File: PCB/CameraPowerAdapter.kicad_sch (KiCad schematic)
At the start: 1 part, among them U1 LT8390EFE#PBF

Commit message: Updated Schematic
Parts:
- added C10, C16, C17, C9: C, symbol Device:C
- added C11, C12, C13, C14: 100n, symbol Device:C
- added C15: 4.7u, symbol Device:C
- added C8: 1u, symbol Device:C
- added L1: L, symbol Device:L
- added Q3, Q4, Q5, Q6: NCEP40T11G, easyeda2kicad:DFN-8_L5.1-W5.7-P1.27-LS6.1-BL, symbol easyeda2kicad:NCEP40T11G
- added R10: 499k, symbol Device:R
- added R5: R, symbol Device:R
- added R8: 365k, symbol Device:R
- added R9: 56.2k, symbol Device:R
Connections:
- net GND: now reaches U1.10 (TEST)
- net GND: now also U1.29 (GND), C11.2, C12.2, C13.2, C14.2, C16.2, C17.2, C8.2, C9.2, R9.2
- net at U1.11 (LOADEN): now also U1.12 (Vref), U1.13 (CTRL), C16.1, R10.2
- net at U1.16 (ISMON): now also C17.1
- net PGOOD: now reaches U1.17 (PGOOD)
- net at U1.18 (SS): now also C9.1, R10.1
- net RT: now reaches U1.21 (RT)
- net SYNC/SPRD: now reaches U1.22 (SYNC/SPRD)
- net SYNC/SPRD: now also C15.1
- net INTVcc: now reaches U1.8 (INTVcc)
- net INTVcc: now also C15.2
- net BG1: now reaches U1.1 (BG1)
- net BG1: now also Q4.4 (G)
- net ISP: now reaches U1.14 (ISP)
- net ISN: now reaches U1.15 (ISN)
- net FB: now reaches U1.19 (FB)
- net at U1.2 (BST1): now also C10.2
- net TG2: now reaches U1.25 (TG2)
- net SW2: now reaches U1.26 (SW2)
- net SW2: now also L1.2
- net BST2: now reaches U1.27 (BST2)
- net BG2: now reaches U1.28 (BG2)
- net SW1: now reaches U1.3 (SW1)
- net SW1: now also U1.5 (LSP), C10.1, Q3.4 (G), R5.1
- net TG1: now reaches U1.4 (TG1)
- net TG1: now also Q6.4 (G)
- net at U1.6 (LSN): now also L1.1, R5.2
- net VOUT: now reaches U1.7 (Vin)
- net VOUT: now also C11.1, C12.1, C13.1, C14.1, C8.1, R8.1
- net EN/UVLO: now reaches U1.9 (EN/UVLO)
- net EN/UVLO: now also R8.2, R9.1
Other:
- note added: "Boost Side"
- note added: "Buck Side"

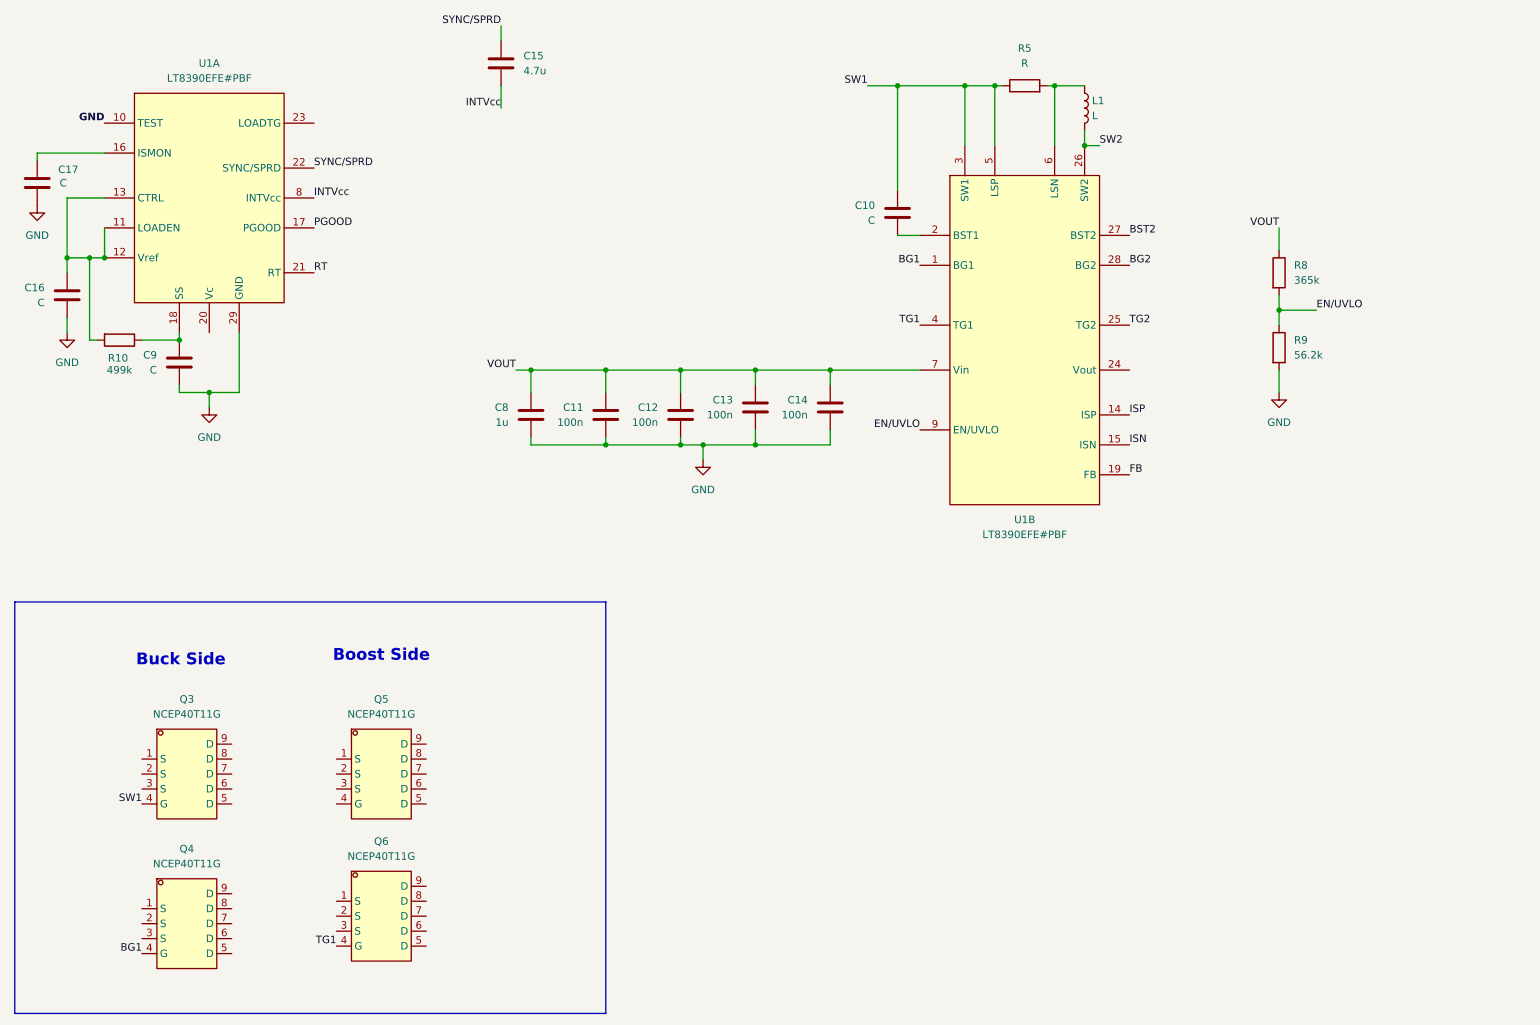
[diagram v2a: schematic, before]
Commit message: Updated topology files to be more readable & BuckBoost schematic updated
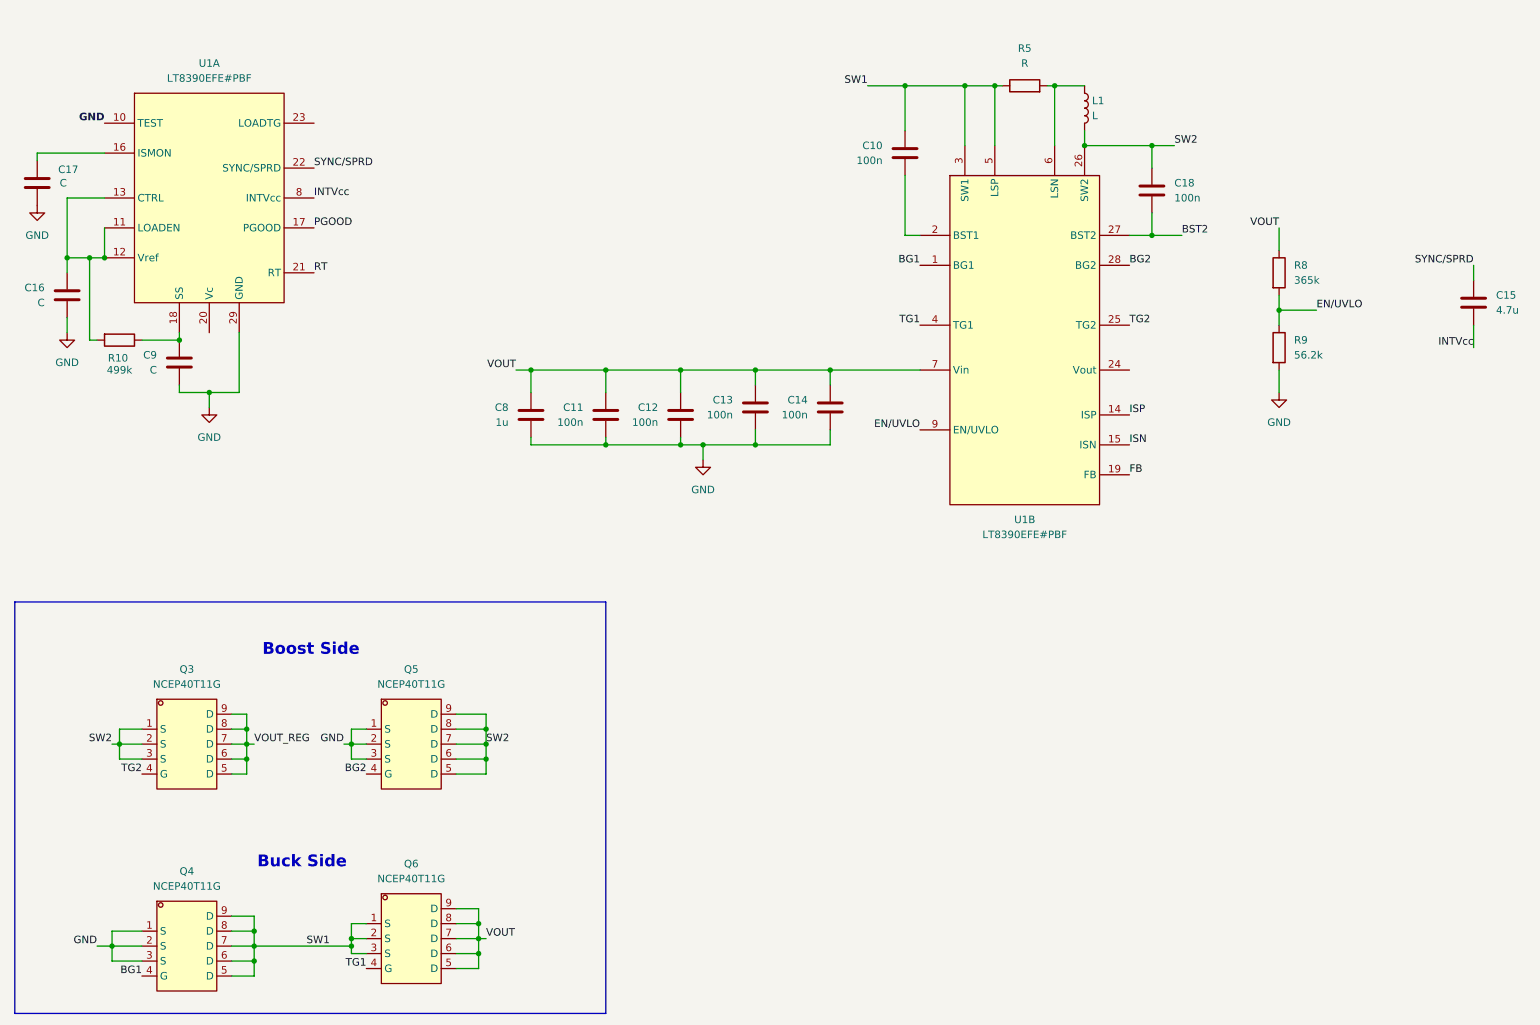
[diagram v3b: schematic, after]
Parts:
- added C18: 100n, symbol Device:C
- C10: value C -> 100n
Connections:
- net BG2: now also Q5.4 (G)
- net BST2: now also C18.2
- net GND: now also Q4.1 (S), Q4.2 (S), Q4.3 (S), Q5.1 (S), Q5.2 (S), Q5.3 (S)
- net SW1: now also Q4.5 (D), Q4.6 (D), Q4.7 (D), Q4.8 (D), Q4.9 (D), Q6.1 (S), Q6.2 (S), Q6.3 (S); no longer Q3.4 (G)
- net SW2: now also Q3.1 (S), Q3.2 (S), Q3.3 (S), Q5.5 (D), Q5.6 (D), Q5.7 (D), Q5.8 (D), Q5.9 (D), C18.1
- net TG2: now also Q3.4 (G)
- net VOUT: now also Q6.5 (D), Q6.6 (D), Q6.7 (D), Q6.8 (D), Q6.9 (D)
- net VOUT_REG: now reaches Q3.5 (D)
- net VOUT_REG: now also Q3.6 (D), Q3.7 (D), Q3.8 (D), Q3.9 (D)
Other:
- moved on the sheet: C10, C15, Q3, Q4, Q5, Q6

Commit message: Added schematic changes
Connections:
- net VOUT_REG: now also U1.24 (Vout)
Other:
- moved on the sheet: C15
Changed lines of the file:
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@@
+	(wire
+		(pts
+			(xy 207.01 81.28) (xy 212.09 81.28)
+		)
+		(stroke
+			(width 0)
+			(type default)
+		)
+	)
 	(wire
 		(pts
@@
 	(wire
 		(pts
-			(xy 265.43 73.66) (xy 265.43 77.47)
+			(xy 93.98 54.61) (xy 93.98 58.42)
 		)
 		(stroke
@@
 	(wire
 		(pts
-			(xy 265.43 63.5) (xy 265.43 66.04)
+			(xy 93.98 44.45) (xy 93.98 46.99)
 		)
 		(stroke
@@
 		)
 	)
+	(label "VOUT_REG"
+		(at 212.09 81.28 0)
+		(effects
+			(font
+				(size 1.27 1.27)
+			)
+			(justify left bottom)
+		)
+	)
 	(label "TG1"
 		(at 171.45 73.66 180)
@@
 	)
 	(label "SYNC/SPRD"
-		(at 265.43 63.5 180)
+		(at 93.98 44.45 180)
 		(effects
 			(font
@@
 	)
 	(label "INTVcc"
-		(at 265.43 77.47 180)
+		(at 93.98 58.42 180)
 		(effects
 			(font
@@
 	(symbol
 		(lib_id "Device:C")
-		(at 265.43 69.85 0)
+		(at 93.98 50.8 0)
 		(unit 1)
 		(body_style 1)
@@
 		(fields_autoplaced yes)
 		(property "Reference" "C15"
-			(at 269.24 68.5799 0)
+			(at 97.79 49.5299 0)
 			(show_name no)
 			(do_not_autoplace no)
@@
 		)
 		(property "Value" "4.7u"
-			(at 269.24 71.1199 0)
+			(at 97.79 52.0699 0)
 			(show_name no)
 			(do_not_autoplace no)
@@
 		)
 		(property "Footprint" ""
-			(at 266.3952 73.66 0)
+			(at 94.9452 54.61 0)
 			(hide yes)
 			(show_name no)
@@
 		)
 		(property "Datasheet" ""
-			(at 265.43 69.85 0)
+			(at 93.98 50.8 0)
 			(hide yes)
 			(show_name no)
@@
 		)
 		(property "Description" "Unpolarized capacitor"
-			(at 265.43 69.85 0)
+			(at 93.98 50.8 0)
 			(hide yes)
 			(show_name no)

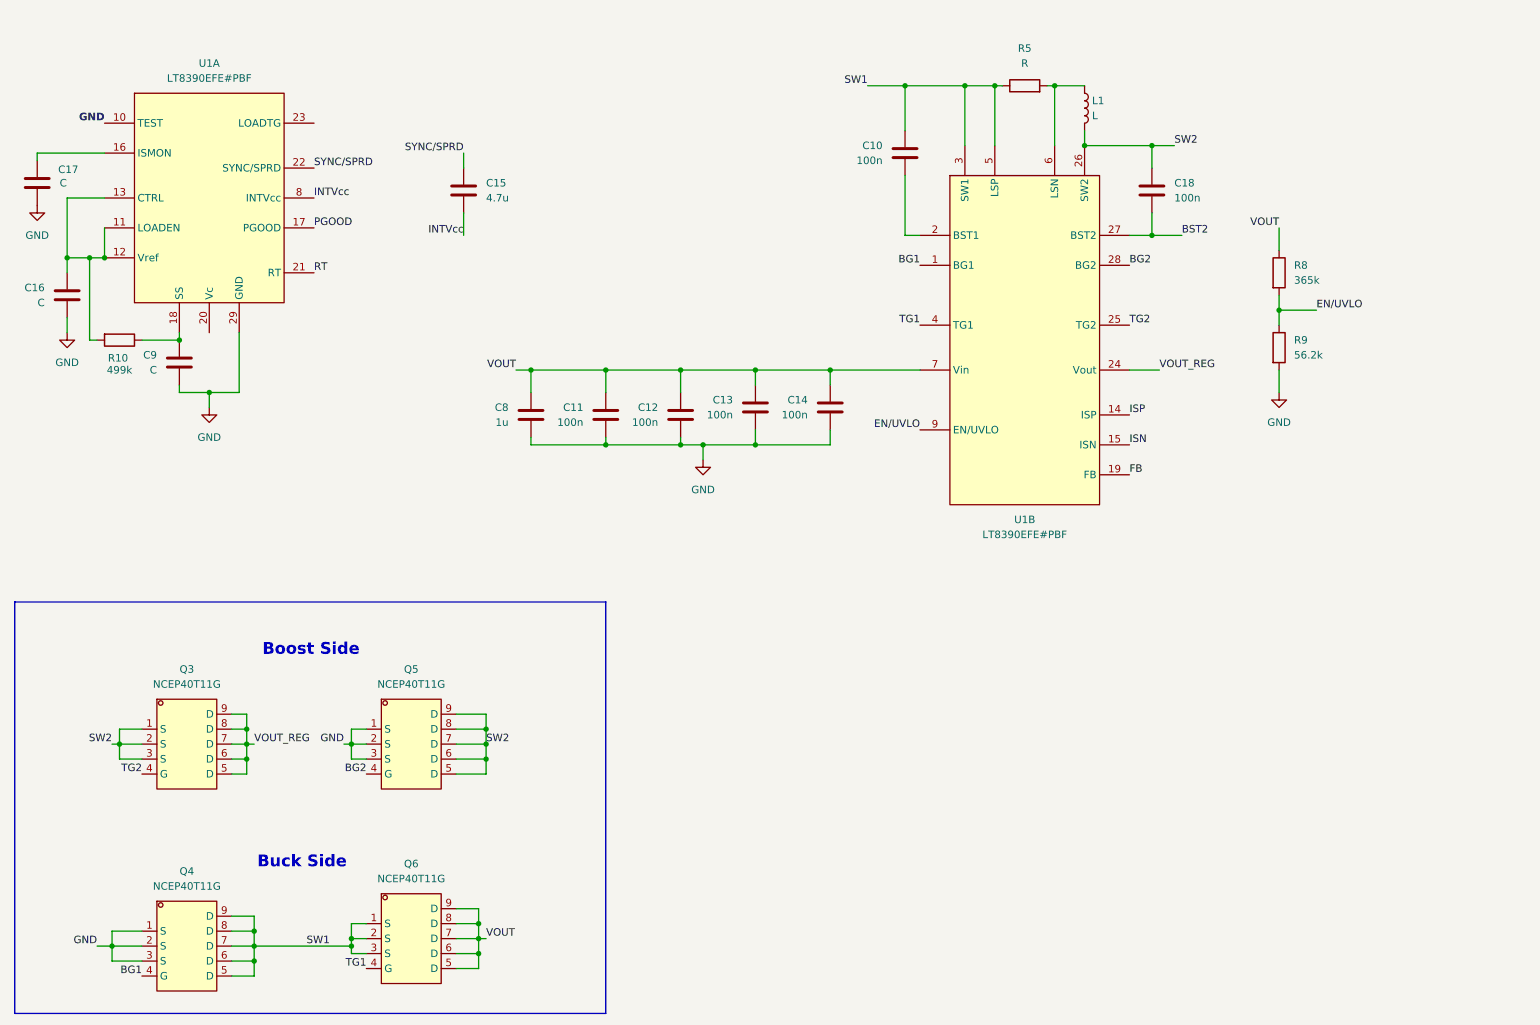
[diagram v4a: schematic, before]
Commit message: Cleaned up schematic
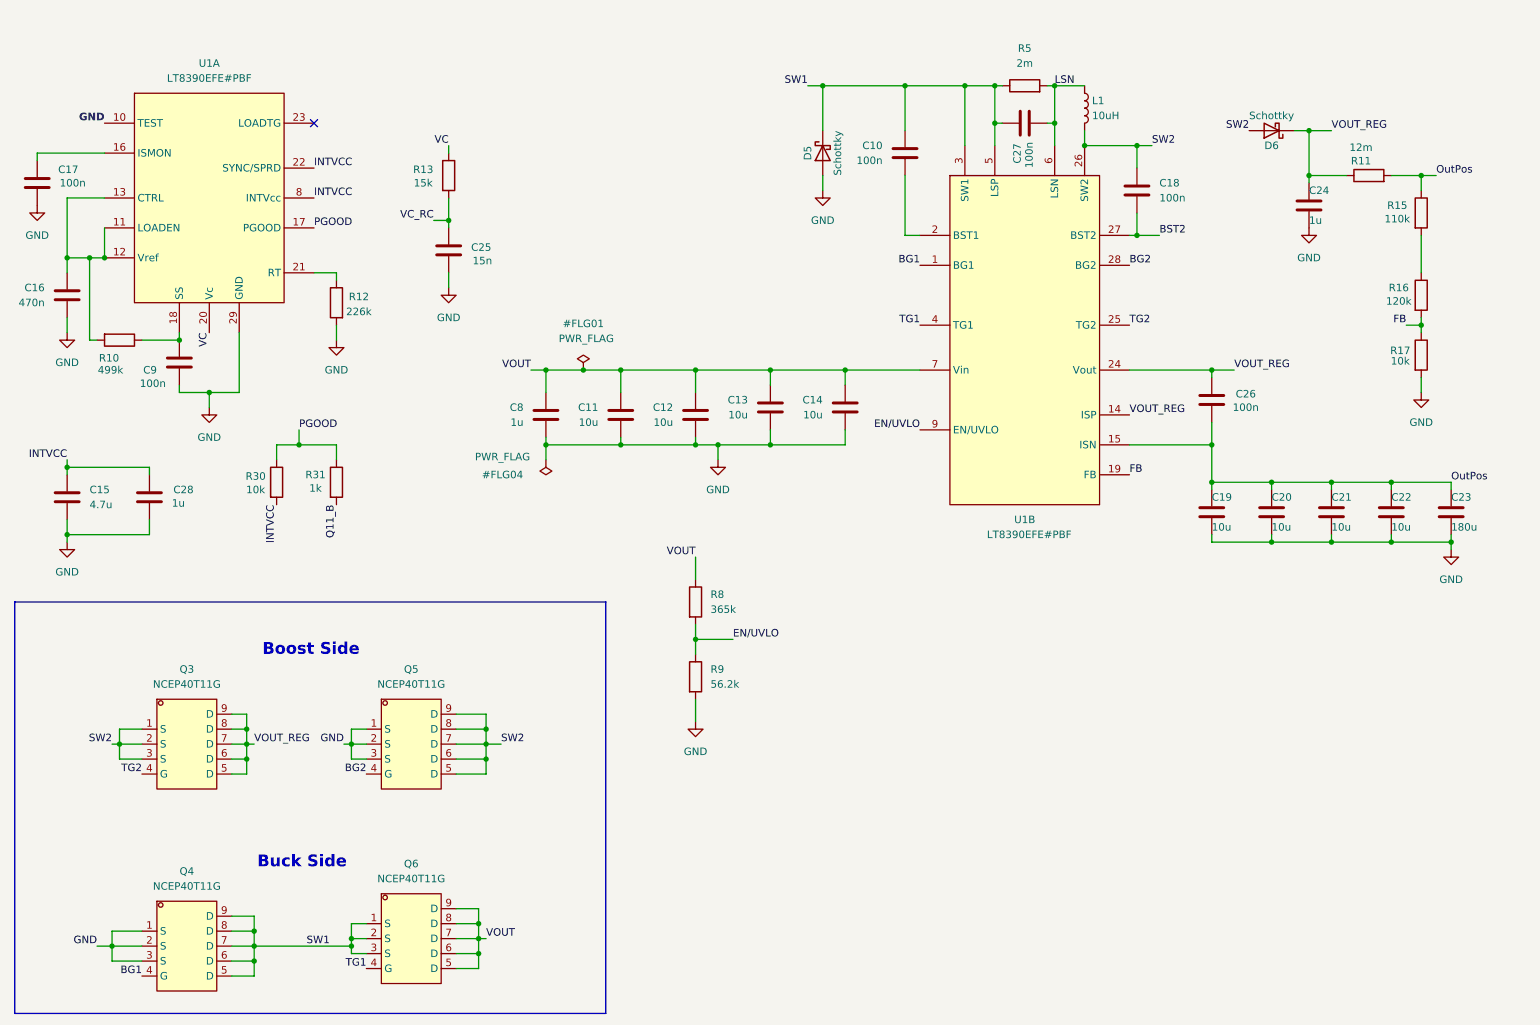
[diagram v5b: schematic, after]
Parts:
- added C19, C20, C21, C22: 10u, symbol Device:C
- added C23: 180u, symbol Device:C
- added C24, C28: 1u, symbol Device:C
- added C25: 15n, symbol Device:C
- added C26, C27: 100n, symbol Device:C
- added D5, D6: Schottky, symbol Device:D_Schottky
- added R11: 12m, symbol Device:R
- added R12: 226k, symbol Device:R
- added R13: 15k, symbol Device:R
- added R15: 110k, symbol Device:R
- added R16: 120k, symbol Device:R
- added R17, R30: 10k, symbol Device:R
- added R31: 1k, symbol Device:R
- C11, C12, C13, C14: value 100n -> 10u
- C16: value C -> 470n
- C17, C9: value C -> 100n
- L1: value L -> 10uH
- R5: value R -> 2m
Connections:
- net ISP is gone; now on net VOUT_REG: U1.14 (ISP)
- net SYNC/SPRD is gone; now on net INTVCC: C15.1, U1.22 (SYNC/SPRD)
- net FB: now also R16.2, R17.1
- net GND: now also C15.2, C19.2, C20.2, C21.2, C22.2, C23.2, C24.2, C25.2, C28.2, D5.2 (A), R12.2, R17.2
- net PGOOD: now also R30.1, R31.1
- net SW1: now also C27.1, D5.1 (K)
- net SW2: now also D6.2 (A)
- net VOUT_REG: now also C24.1, C26.1, D6.1 (K), R11.1
- net LSN: now reaches L1.1, R5.2, U1.6 (LSN)
- net LSN: now also C27.2
- net VC: now reaches U1.20 (Vc)
- net VC: now also R13.1
- net INTVcc renamed INTVCC
- net INTVCC: now also C28.1, R30.2; no longer C15.2
- net ISN renamed OutPos
- net OutPos: now also C19.1, C20.1, C21.1, C22.1, C23.1, C26.2, R11.2, R15.1
- net RT: no longer names the net of U1.21 (RT)
- net RT: now also R12.1
- new net: R15.2, R16.1
- new net Q11_B: R31.2
- new net VC_RC: C25.1, R13.2
- no-connect marks 0 -> 1
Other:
- moved on the sheet: C11, C12, C13, C14, C15, C18, C8

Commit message: Updated schematic and created 3D assembly to check mechanical clearances and review with Thomas.
To-do, clarify where the input and output ports should be.
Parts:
- added HS1, HS2: Heatsink_Pad, easyeda2kicad:Heatsink_20x20x10_XSD271-294, symbol Mechanical:Heatsink_Pad
- C10, C11, C12, C13, C14, C15, C16, C17, C18, C19, C20, C21, C22, C23, C24, C25, C26, C27, C28, C8, C9: footprint (none) -> Capacitor_SMD:C_0603_1608Metric
- D5, D6: footprint (none) -> Diode_SMD:D_0805_2012Metric
- L1: footprint (none) -> Inductor_THT:Choke_EPCOS_B82722A
- R10, R11, R12, R13, R15, R16, R17, R30, R31, R5, R8, R9: footprint (none) -> Resistor_SMD:R_0603_1608Metric
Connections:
- net SW1: now also HS2.1
- net SW2: now also HS1.1
- net VOUT renamed Vmux
